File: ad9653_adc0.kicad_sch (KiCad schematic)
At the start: 20 parts, among them J201 142-0701-201, J202 142-0701-201, J203 142-0701-201, J204 142-0701-201, U201 AD9653BCPZ-125

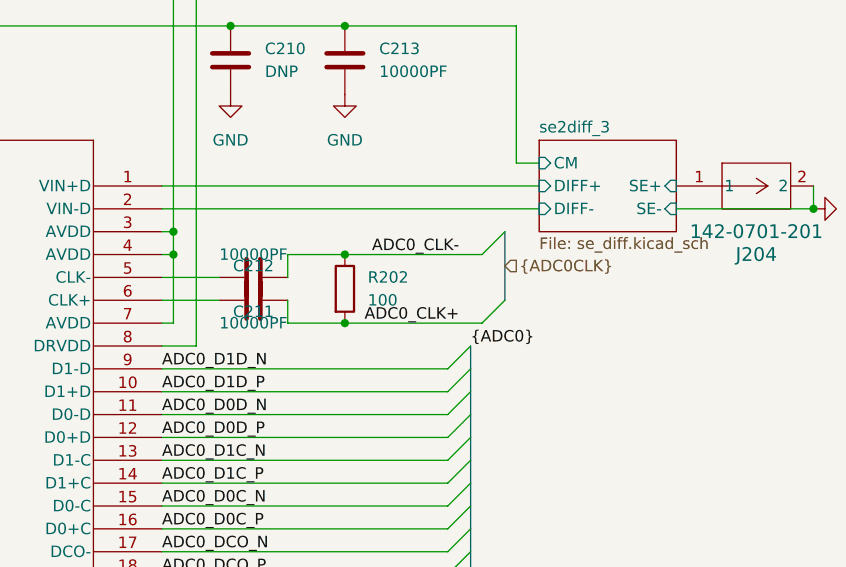
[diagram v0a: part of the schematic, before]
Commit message: fixed differential pair impedance and length matching. Also fixed DRC errors (trace spacing). These are only layout changes, the schematic remains unchanged.
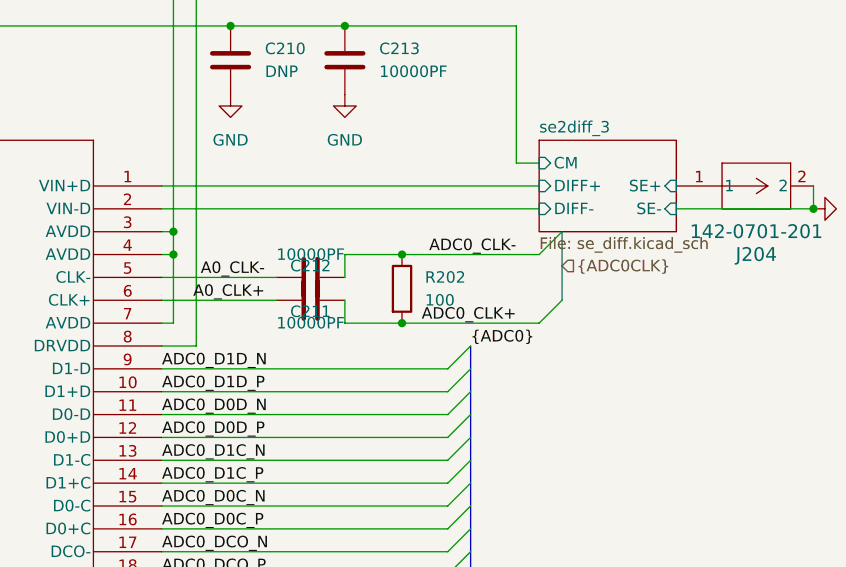
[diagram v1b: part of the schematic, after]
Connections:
- net A0_CLK-: now reaches C211.2, U201.5 (CLK-)
- net A0_CLK+: now reaches C212.2, U201.6 (CLK+)
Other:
- moved on the sheet: C211, C212, R202
